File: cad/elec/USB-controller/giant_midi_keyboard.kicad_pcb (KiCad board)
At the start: 2 copper layers, 116.8 x 57.1 mm, 31 parts, among them P1 LEFT, P2 RIGHT, U1 MCP3008, U2 MCP3008, U3 MCP3008, U4 MCP3008, U5 ARDUINO_MICRO

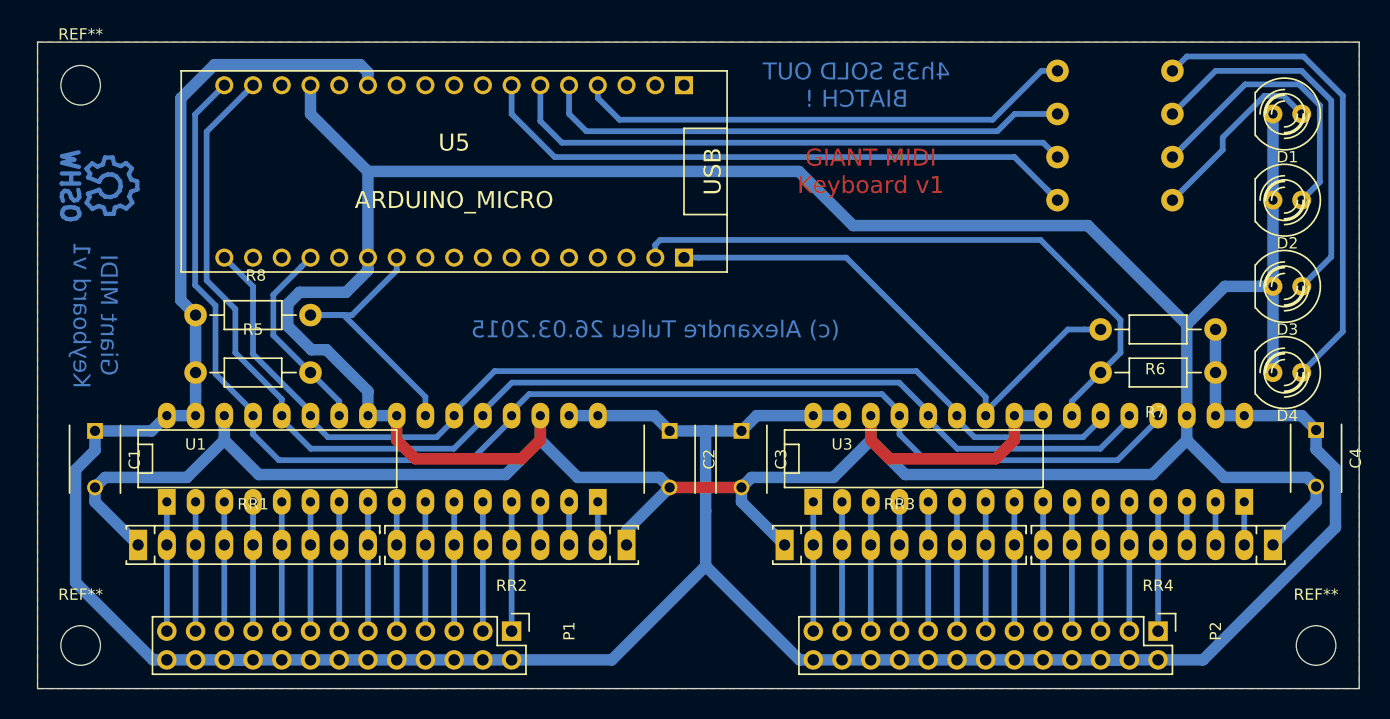
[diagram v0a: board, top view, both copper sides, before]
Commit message: Updates usb board for use with panel board
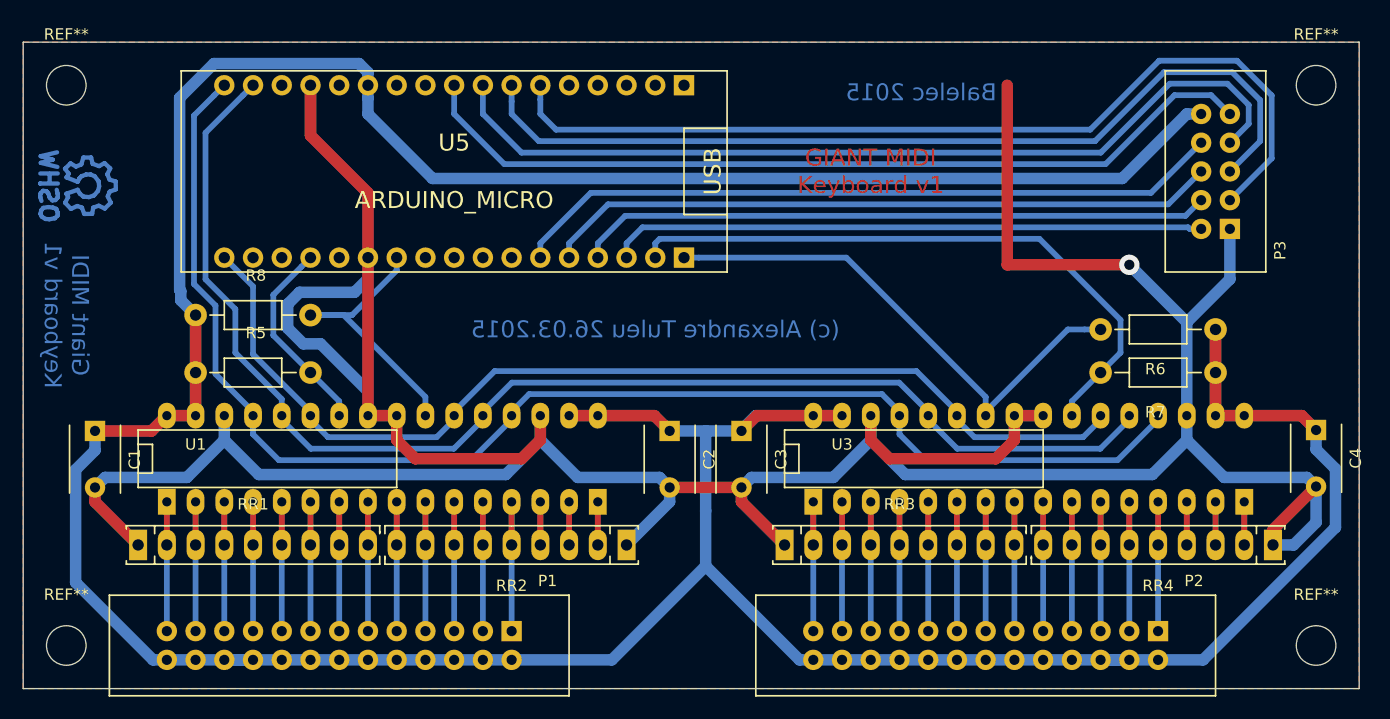
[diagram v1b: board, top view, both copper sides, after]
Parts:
- removed D1, D2, D3, D4: LED, LEDs:LED-5MM
- removed R1, R2, R3, R4: 100, Resistors_ThroughHole:Resistor_Horizontal_RM10mm
- added P3: CONN_01X10, Giant_Midi_Keyboard:Header_2x5, F.Cu at (181.6, 105.4)
- added REF**: MountingHole_3-5mm, Mounting_Holes:MountingHole_3-5mm, F.Cu at (190.5, 97.8)
- P1, P2: footprint Pin_Headers:Pin_Header_Straight_2x13 -> Giant_Midi_Keyboard:Header_2x13
- moved P2 15.3 mm to (161.3, 147.3), turned to 90 degrees
- moved P1 15.3 mm to (104.1, 147.3), turned to 90 degrees
- moved REF** 1.90 mm to (81.9, 106.7)
- moved REF** 1.27 mm to (80.0, 97.8)
- moved REF** 1.27 mm to (80.0, 147.3)
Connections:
- U5 pad 12: Net-(U5-Pad12) -> /DBG_I1
- U5 pad 13: Net-(U5-Pad13) -> /DBG_O0
- U5 pad 14: Net-(U5-Pad14) -> /DBG_O2
- U5 pad 15: Net-(U5-Pad15) -> /DBG_O4
- U5 pad 21: /DBG3 -> Net-(U5-Pad21)
- U5 pad 22: /DBG2 -> Net-(U5-Pad22)
- U5 pad 23: /DBG1 -> /DBG_O3
- U5 pad 24: /DBG0 -> /DBG_O1
- U5 pad 25: Net-(U5-Pad25) -> /DBG_I2
- U5 pad 26: Net-(U5-Pad26) -> /DBG_I0
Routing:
- net +5V: track 265.9 -> 401.4 mm
- net /DBG_O3: track 0.00 -> 82.4 mm
- net /DBG_O1: track 0.00 -> 80.7 mm
- net /DBG_I2: track 0.00 -> 79.0 mm
- net /DBG_I0: track 0.00 -> 76.2 mm
- net /DBG_I1: track 0.00 -> 63.4 mm
- net /DBG_O0: track 0.00 -> 59.8 mm
- net /DBG_O2: track 0.00 -> 56.2 mm
- net /DBG0: track 55.4 -> 0.00 mm
- net /DBG_O4: track 0.00 -> 52.7 mm
- net /DBG1: track 50.2 -> 0.00 mm
- net /DBG2: track 47.0 -> 0.00 mm
- net /DBG3: track 44.4 -> 0.00 mm
- net Net-(D4-Pad1): track 43.0 -> 0.00 mm
- net Net-(D3-Pad1): track 34.2 -> 0.00 mm
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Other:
- board size 116.8 x 57.1 mm -> 118.1 x 57.1 mm
- board text added: "Balelec 2015"
- board text removed: "4h35 SOLD OUT BIATCH !"
